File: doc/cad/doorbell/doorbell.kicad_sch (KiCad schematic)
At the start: 23 parts, among them J1 Doorbell PCB, J2 12V Supply, J3 Speaker, T1 Transformer_1P_1S, U1 ESP32-WROOM-32, U2 TDA1517P/N3_112, U3 AMS1117-3.3

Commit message: Designing pcb
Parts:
- C1: footprint (none) -> Capacitor_THT:CP_Radial_D4.0mm_P1.50mm
- C10: footprint (none) -> Capacitor_THT:CP_Radial_D12.5mm_P5.00mm
- C11, C12: value 0.1 uF -> 100 nF; footprint (none) -> Capacitor_THT:C_Disc_D10.0mm_W2.5mm_P5.00mm
- C2, C5: footprint (none) -> Capacitor_THT:CP_Radial_D5.0mm_P2.00mm
- C3: footprint (none) -> Capacitor_THT:C_Disc_D6.0mm_W2.5mm_P5.00mm
- C4: footprint (none) -> Capacitor_THT:CP_Radial_D5.0mm_P2.00mm; symbol Device:C -> Device:C_Polarized
- C6: footprint (none) -> Capacitor_THT:CP_Radial_D10.0mm_P3.80mm
- C7, C9: footprint Package_DIP:DIP-16_W7.62mm -> Capacitor_THT:C_Disc_D10.0mm_W2.5mm_P5.00mm
- C8: footprint (none) -> Capacitor_THT:C_Disc_D10.0mm_W2.5mm_P5.00mm
- J1: footprint (none) -> Connector_JST:JST_PH_B7B-PH-K_1x07_P2.00mm_Vertical
- J2, J3: footprint (none) -> Connector_JST:JST_PH_B2B-PH-K_1x02_P2.00mm_Vertical
- R1, R2, R3: footprint (none) -> Resistor_THT:R_Axial_DIN0207_L6.3mm_D2.5mm_P10.16mm_Horizontal
- RV1: footprint (none) -> Potentiometer_THT:Potentiometer_Piher_PT-10-V10_Vertical_Hole
- T1: footprint (none) -> Transformer_THT:Transformer_NF_ETAL_P1165
- U2: footprint SOT398-1_NXP -> Package_DIP:DIP-18_W7.62mm
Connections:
- net at C7.1, U2.1 (-INV1): now also C4.2; no longer C4.1
- net at R2.1: now also C4.1; no longer C4.2
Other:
- moved on the sheet: C1, C10, C11, C12, C2, C3, C5, C6, C7, C8, C9, J1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

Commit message: updated pcb
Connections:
- net +3.3V: now reaches C12.1, C2.1, J1.1 (Pin_1), R3.1, U1.2 (VDD), U3.2 (VO)
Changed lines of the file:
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@@
+	(wire
+		(pts
+			(xy 104.14 33.02) (xy 104.14 35.56)
+		)
+		(stroke
+			(width 0)
+			(type default)
+		)
+	)
 	(wire
 		(pts
@@
 					(unit 1)
 				)
+			)
+		)
+	)
+	(symbol
+		(lib_id "power:+3.3V")
+		(at 104.14 33.02 0)
+		(unit 1)
+		(body_style 1)
+		(exclude_from_sim no)
+		(in_bom yes)
+		(on_board yes)
+		(in_pos_files yes)
+		(dnp no)
+		(fields_autoplaced yes)
+		(property "Reference" "#PWR010"
+			(at 104.14 36.83 0)
+			(hide yes)
+			(show_name no)
+			(do_not_autoplace no)
+			(effects
+				(font
+					(size 1.27 1.27)
+				)
+			)
+		)
+		(property "Value" "+3.3V"
+			(at 104.14 27.94 0)
+			(show_name no)
+			(do_not_autoplace no)
+			(effects
+				(font
+					(size 1.27 1.27)
+				)
+			)
+		)
+		(property "Footprint" ""
+			(at 104.14 33.02 0)
+			(hide yes)
+			(show_name no)
+			(do_not_autoplace no)
+			(effects
+				(font
+					(size 1.27 1.27)
+				)
+			)
+		)
+		(property "Datasheet" ""
+			(at 104.14 33.02 0)
+			(hide yes)
+			(show_name no)
+			(do_not_autoplace no)
+			(effects
+				(font
+					(size 1.27 1.27)
+				)
+			)
+		)
+		(property "Description" "Power symbol creates a global label with name \"+3.3V\""
+			(at 104.14 33.02 0)
+			(hide yes)
+			(show_name no)
+			(do_not_autoplace no)
+			(effects
+				(font
+					(size 1.27 1.27)
+				)
+			)
+		)
+		(pin "1"
+		)
+		(instances
+			(project "doorbell"
+				(path "/f683d8ac-5508-440b-b2f3-b92d22a6af2a"
+					(reference "#PWR010")
+					(unit 1)
+				)

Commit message: Minor improvements
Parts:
- RV1: footprint Potentiometer_THT:Potentiometer_Piher_PT-10-V10_Vertical_Hole -> Potentiometer_THT:Potentiometer_Piher_PT-15-H05_Horizontal
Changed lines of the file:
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@@
 			)
 		)
-		(property "Footprint" "Potentiometer_THT:Potentiometer_Piher_PT-10-V10_Vertical_Hole"
+		(property "Footprint" "Potentiometer_THT:Potentiometer_Piher_PT-15-H05_Horizontal"
 			(at 142.24 127 0)
 			(hide yes)

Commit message: Added testing hackRF rf captures. Schematic updates.
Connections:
- net at T1.1 (AA): now also J1.7 (Pin_7); no longer J1.5 (Pin_5)
- net at T1.2 (AB): now also J1.6 (Pin_6); no longer J1.4 (Pin_4)
- net at U1.28 (IO17): now also J1.5 (Pin_5)
- net at U1.30 (IO18): now also J1.4 (Pin_4)
- no-connect marks 33 -> 29
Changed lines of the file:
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@@
-	)
-	(no_connect
-		(at 152.4 34.29)
-	)
-	(no_connect
-		(at 97.79 113.03)
 	)
 	(no_connect
@@
 	)
 	(no_connect
-		(at 97.79 110.49)
-	)
-	(no_connect
 		(at 67.31 123.19)
 	)
@@
 	)
 	(no_connect
-		(at 149.86 34.29)
-	)
-	(no_connect
 		(at 67.31 125.73)
 	)
@@
 	(wire
 		(pts
+			(xy 116.84 113.03) (xy 116.84 58.42)
+		)
+		(stroke
+			(width 0)
+			(type default)
+		)
+	)
+	(wire
+		(pts
 			(xy 85.09 52.07) (xy 85.09 43.18)
 		)
@@
 	(wire
 		(pts
-			(xy 147.32 34.29) (xy 147.32 69.85)
-		)
-		(stroke
-			(width 0)
-			(type default)
-		)
-	)
-	(wire
-		(pts
 			(xy 182.88 116.84) (xy 201.93 116.84)
 		)
@@
 	(wire
 		(pts
-			(xy 144.78 34.29) (xy 144.78 66.04)
-		)
-		(stroke
-			(width 0)
-			(type default)
-		)
-	)
-	(wire
-		(pts
 			(xy 191.77 26.67) (xy 72.39 26.67)
 		)
@@
 	(wire
 		(pts
+			(xy 97.79 113.03) (xy 116.84 113.03)
+		)
+		(stroke
+			(width 0)
+			(type default)
+		)
+	)
+	(wire
+		(pts
 			(xy 44.45 93.98) (xy 44.45 97.79)
 		)
@@
 	(wire
 		(pts
+			(xy 137.16 66.04) (xy 149.86 66.04)
+		)
+		(stroke
+			(width 0)
+			(type default)
+		)
+	)
+	(wire
+		(pts
 			(xy 137.16 34.29) (xy 137.16 35.56)
 		)
@@
 	(wire
 		(pts
+			(xy 97.79 110.49) (xy 120.65 110.49)
+		)
+		(stroke
+			(width 0)
+			(type default)
+		)
+	)
+	(wire
+		(pts
 			(xy 72.39 52.07) (xy 72.39 59.69)
 		)
@@
 	(wire
 		(pts
+			(xy 120.65 110.49) (xy 120.65 60.96)
+		)
+		(stroke
+			(width 0)
+			(type default)
+		)
+	)
+	(wire
+		(pts
+			(xy 120.65 60.96) (xy 147.32 60.96)
+		)
+		(stroke
+			(width 0)
+			(type default)
+		)
+	)
+	(wire
+		(pts
 			(xy 146.05 96.52) (xy 147.32 96.52)
 		)
@@
 	(wire
 		(pts
+			(xy 147.32 69.85) (xy 152.4 69.85)
+		)
+		(stroke
+			(width 0)
+			(type default)
+		)
+	)
+	(wire
+		(pts
 			(xy 201.93 129.54) (xy 201.93 143.51)
 		)
@@
 	(wire
 		(pts
-			(xy 137.16 66.04) (xy 137.16 69.85)
-		)
-		(stroke
-			(width 0)
-			(type default)
-		)
-	)
-	(wire
-		(pts
 			(xy 128.27 63.5) (xy 128.27 104.14)
 		)
@@
 	(wire
 		(pts
+			(xy 116.84 58.42) (xy 144.78 58.42)
+		)
+		(stroke
+			(width 0)
+			(type default)
+		)
+	)
+	(wire
+		(pts
 			(xy 185.42 34.29) (xy 185.42 48.26)
 		)
@@
 	(wire
 		(pts
+			(xy 147.32 60.96) (xy 147.32 34.29)
+		)
+		(stroke
+			(width 0)
+			(type default)
+		)
+	)
+	(wire
+		(pts
 			(xy 137.16 127) (xy 137.16 111.76)
 		)
@@
 	(wire
 		(pts
-			(xy 137.16 66.04) (xy 144.78 66.04)
-		)
-		(stroke
-			(width 0)
-			(type default)
-		)
-	)
-	(wire
-		(pts
 			(xy 104.14 33.02) (xy 104.14 35.56)
 		)
@@
 	(wire
 		(pts
+			(xy 144.78 58.42) (xy 144.78 34.29)
+		)
+		(stroke
+			(width 0)
+			(type default)
+		)
+	)
+	(wire
+		(pts
 			(xy 96.52 35.56) (xy 96.52 41.91)
 		)
@@
 	(wire
 		(pts
+			(xy 137.16 69.85) (xy 137.16 66.04)
+		)
+		(stroke
+			(width 0)
+			(type default)
+		)
+	)
+	(wire
+		(pts
 			(xy 138.43 127) (xy 137.16 127)
 		)
@@
 	(wire
 		(pts
+			(xy 152.4 69.85) (xy 152.4 34.29)
+		)
+		(stroke
+			(width 0)
+			(type default)
+		)
+	)
+	(wire
+		(pts
 			(xy 182.88 34.29) (xy 182.88 76.2)
 		)
@@
 		)
 		(stroke
+			(width 0)
+			(type default)
+		)
+	)
+	(wire
+		(pts
+			(xy 149.86 66.04) (xy 149.86 34.29)
+		)
+		(stroke

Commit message: Several fixes and improvements
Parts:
- added J4: UART, Connector_PinHeader_2.54mm:PinHeader_1x07_P2.54mm_Vertical, symbol Connector:Conn_01x07_Pin
- added R4: 10K, Resistor_THT:R_Axial_DIN0207_L6.3mm_D2.5mm_P10.16mm_Horizontal, symbol Device:R
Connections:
- net +3.3V: now also J4.7 (Pin_7), R4.1
- net GND: now also J4.2 (Pin_2), J4.6 (Pin_6)
- net SPK+: now reaches J1.7 (Pin_7), T1.1 (AA)
- net SPK-: now reaches J1.6 (Pin_6), T1.2 (AB)
- net RESET: now reaches C11.1, R3.2, U1.3 (EN)
- net RESET: now also J4.1 (Pin_1)
- net BOOT: now reaches U1.25 (IO0)
- net BOOT: now also J4.3 (Pin_3), R4.2
- net at U1.28 (IO17): no longer J1.5 (Pin_5)
- net VOL: now reaches J1.4 (Pin_4), U1.30 (IO18)
- net SONG: now reaches U1.31 (IO19)
- net SONG: now also J1.5 (Pin_5)
- net BELL_WRITE: now reaches J1.3 (Pin_3), R1.1, U1.33 (IO21)
- net RX: now reaches U1.34 (RXD0/IO3)
- net RX: now also J4.5 (Pin_5)
- net TX: now reaches U1.35 (TXD0/IO1)
- net TX: now also J4.4 (Pin_4)
- net BELL_READ: now reaches R1.2, U1.36 (IO22)
- no-connect marks 29 -> 26
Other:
- company: (none) -> creationfactory.co
- title: (none) -> Kinetic Doorbell Wifi Expansion
- moved on the sheet: J1, J3

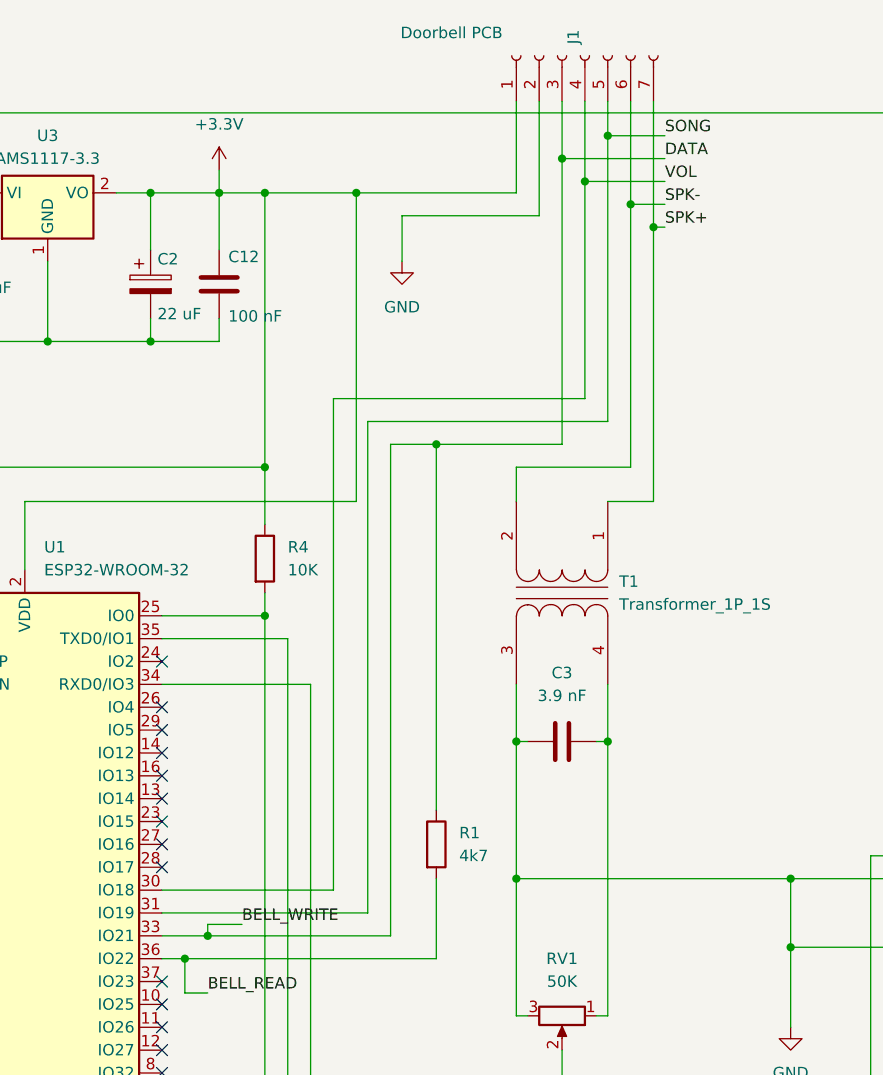
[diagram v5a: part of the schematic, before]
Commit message: Copper area improvements
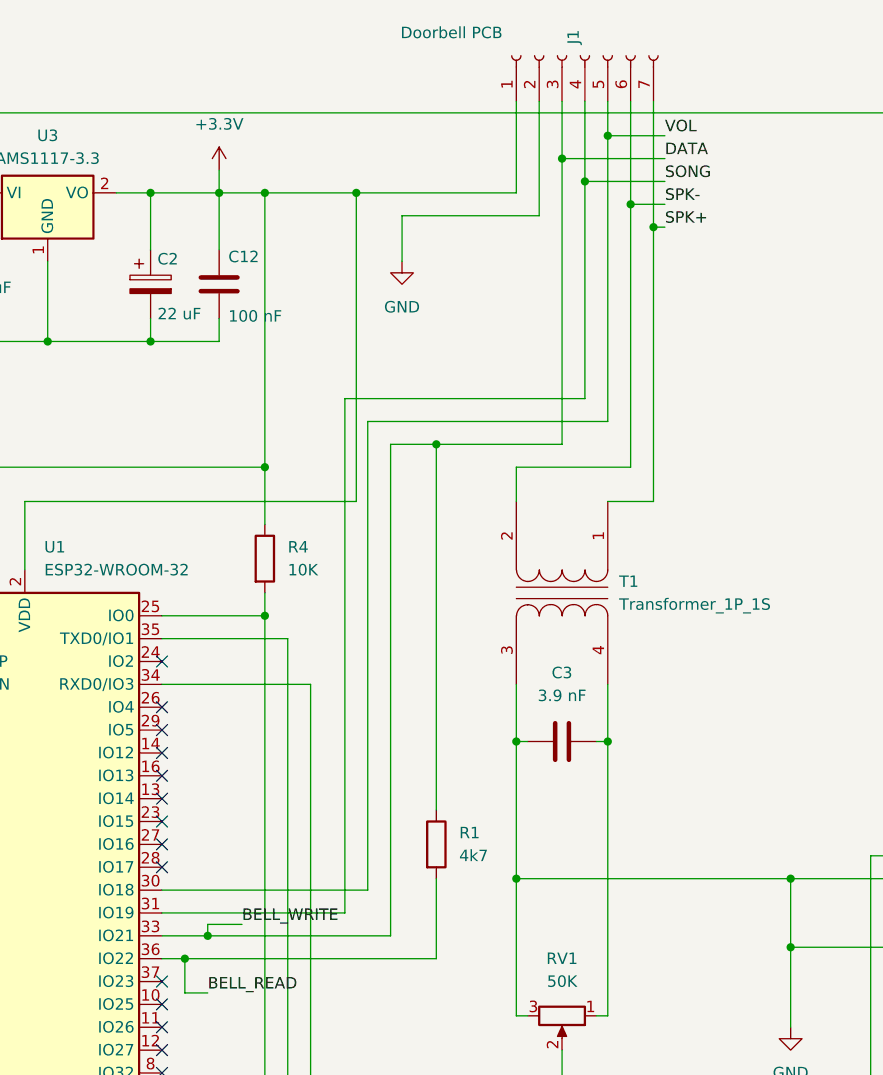
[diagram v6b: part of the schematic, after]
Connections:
- net SONG: now also J1.4 (Pin_4); no longer J1.5 (Pin_5)
- net VOL: now also J1.5 (Pin_5); no longer J1.4 (Pin_4)
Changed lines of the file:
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@@
 	(wire
 		(pts
-			(xy 116.84 113.03) (xy 116.84 58.42)
+			(xy 118.11 58.42) (xy 118.11 115.57)
 		)
 		(stroke
@@
 	(wire
 		(pts
-			(xy 97.79 113.03) (xy 116.84 113.03)
-		)
-		(stroke
-			(width 0)
-			(type default)
-		)
-	)
-	(wire
-		(pts
 			(xy 44.45 93.98) (xy 44.45 97.79)
 		)
@@
 	(wire
 		(pts
+			(xy 118.11 115.57) (xy 97.79 115.57)
+		)
+		(stroke
+			(width 0)
+			(type default)
+		)
+	)
+	(wire
+		(pts
 			(xy 72.39 35.56) (xy 77.47 35.56)
 		)
@@
 	(wire
 		(pts
-			(xy 120.65 60.96) (xy 120.65 115.57)
+			(xy 120.65 60.96) (xy 120.65 113.03)
 		)
 		(stroke
@@
 	(wire
 		(pts
-			(xy 97.79 115.57) (xy 120.65 115.57)
-		)
-		(stroke
-			(width 0)
-			(type default)
-		)
-	)
-	(wire
-		(pts
 			(xy 147.32 69.85) (xy 152.4 69.85)
 		)
@@
 	(wire
 		(pts
-			(xy 116.84 58.42) (xy 144.78 58.42)
+			(xy 118.11 58.42) (xy 144.78 58.42)
 		)
 		(stroke
@@
 		(pts
 			(xy 149.86 25.4) (xy 149.86 36.83)
+		)
+		(stroke
+			(width 0)
+			(type default)
+		)
+	)
+	(wire
+		(pts
+			(xy 97.79 113.03) (xy 120.65 113.03)
 		)
 		(stroke
@@
 		)
 	)
-	(label "VOL"
+	(label "SONG"
 		(at 153.67 34.29 0)
 		(effects
@@
 		)
 	)
-	(label "SONG"
+	(label "VOL"
 		(at 153.67 29.21 0)
 		(effects
